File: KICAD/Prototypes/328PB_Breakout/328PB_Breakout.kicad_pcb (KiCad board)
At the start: 2 copper layers, 32 x 32 mm, 13 parts, among them SW1 SW_PUSH, U1 ATMEGA328PB, U2 AVRISP, U3 FTDI

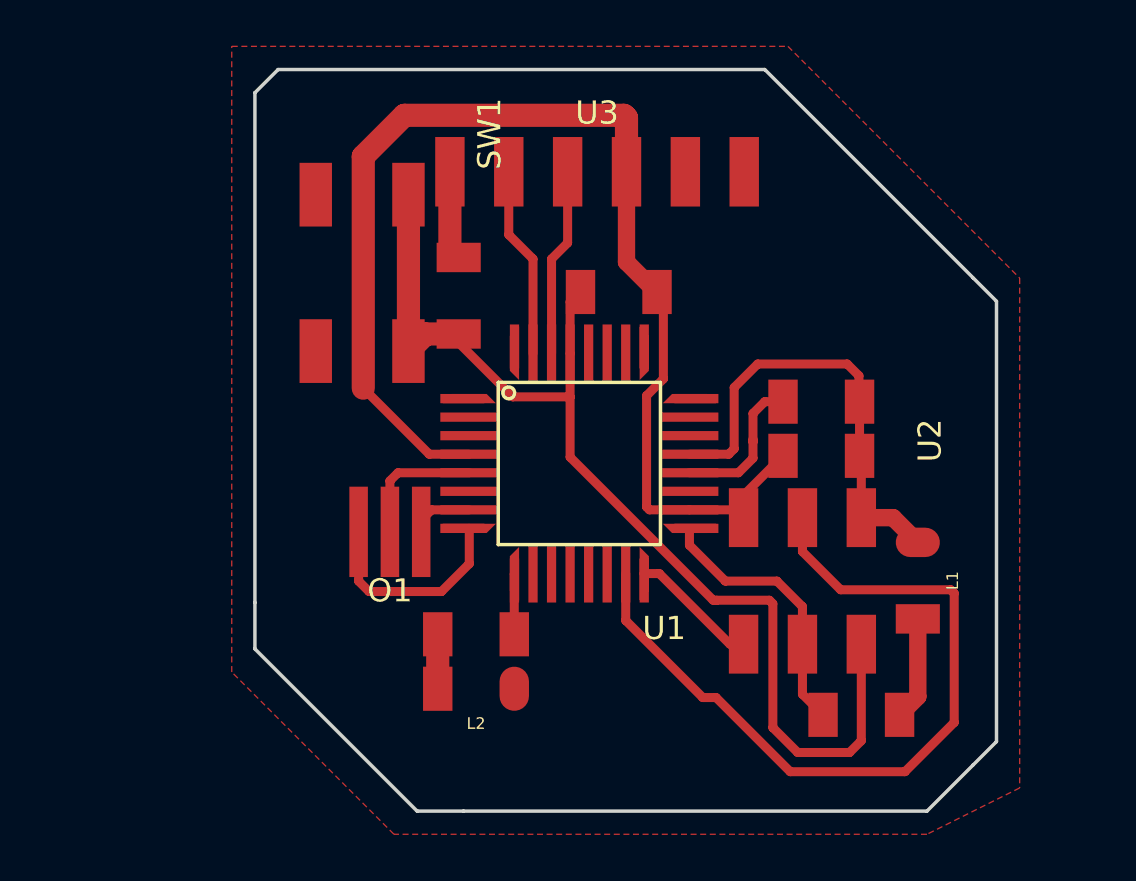
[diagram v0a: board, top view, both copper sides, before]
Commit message: rerouted 328pb breakout
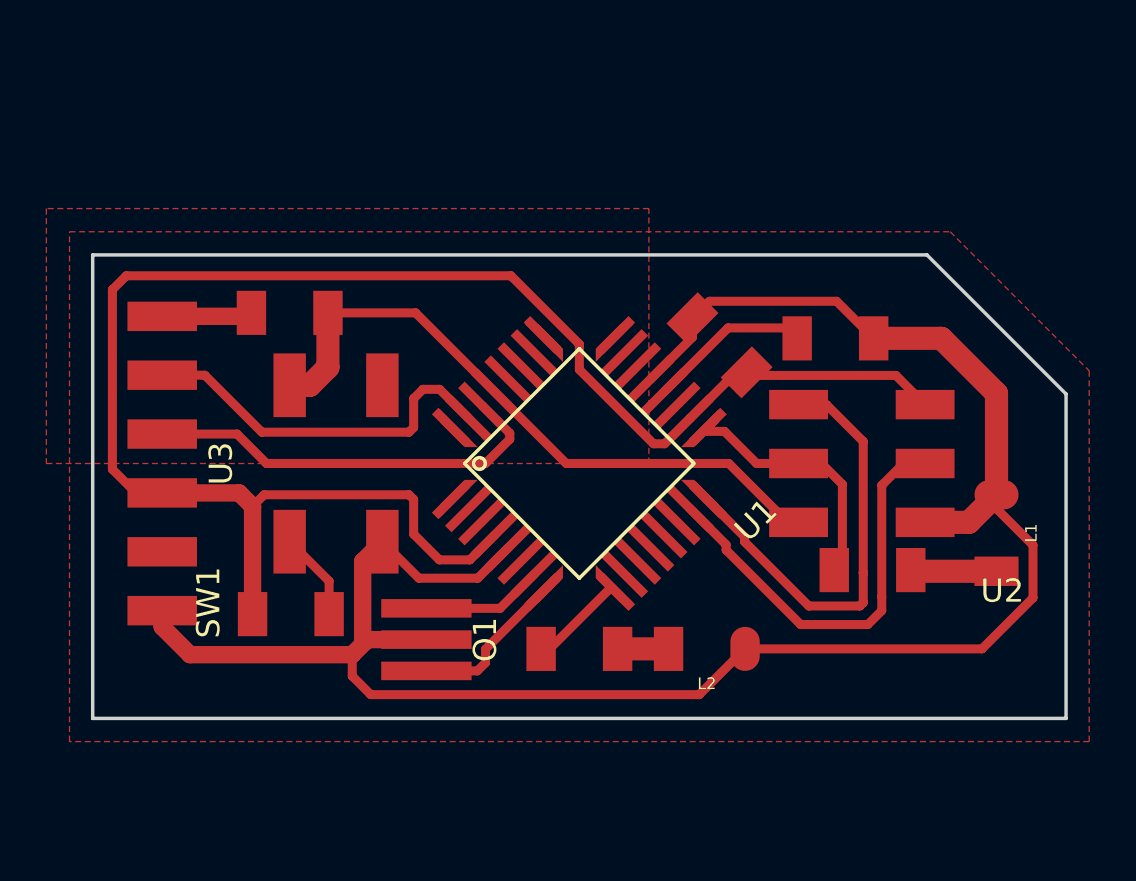
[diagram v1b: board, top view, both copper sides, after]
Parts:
- moved U3 22.6 mm to (82.0, 100.0), turned to 90 degrees
- moved R2 19.8 mm to (87.5, 106.5), turned to 0 degrees
- moved L2 10.1 mm to (105.5, 108.0)
- moved SW1 8.30 mm to (89.5, 100.0), turned to 270 degrees
- moved C3 7.33 mm to (87.5, 93.5), turned to 0 degrees
- moved C1 6.48 mm to (106.0, 94.9), turned to 135 degrees
- moved R1 6.26 mm to (112.7, 104.6)
- moved U2 5.77 mm to (112.0, 100.0), turned to 0 degrees
- moved O1 4.91 mm to (93.4, 107.6), turned to 90 degrees
- moved R3 4.50 mm to (100.0, 108.0), turned to 0 degrees
- moved L1 3.97 mm to (118.0, 103.0)
- moved C2 2.80 mm to (111.0, 94.6)
- turned U1 to 45 degrees
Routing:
- net GND: track 25.5 -> 88.1 mm
- net +5V: track 53.4 -> 73.1 mm
- net RESET: track 48.0 -> 32.2 mm
- net MOSI: track 34.1 -> 18.4 mm
- net MISO: track 5.98 -> 19.5 mm
- net RX: track 8.13 -> 17.9 mm
- net TX: track 8.27 -> 16.3 mm
- net Net-(O1-Pad3): track 2.76 -> 5.27 mm
- net Net-(O1-Pad1): track 9.11 -> 7.06 mm
- net Net-(R3-Pad1): track 2.62 -> 4.13 mm
- net SCK: track 11.7 -> 10.8 mm
- net Net-(L1-Pad1): track 4.47 -> 3.72 mm
- net Net-(C2-Pad1): track 6.54 -> 7.09 mm
- added copper zone on F.Cu, net +5V
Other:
- board size 32 x 32 mm -> 42 x 20 mm
